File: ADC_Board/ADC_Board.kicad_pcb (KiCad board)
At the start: 2 copper layers, 96 x 67.5 mm, 55 parts, among them IC1 UCC12040DVE, IC2 ADS131M04QPWRQ1, IC7 ISO7762FDWR, J1 Conn_01x01_Pin, J2 Conn_01x01_Pin, J3 Conn_01x01_Pin, J4 Conn_01x01_Pin, J5 Conn_01x01_Pin, J6 Conn_01x01_Pin, J7 Conn_01x01_Pin, J8 Conn_01x01_Pin, U1 OPA990IDCKR, U2 OPA990IDCKR, U3 INA210AIDCKR, U4 INA210AIDCKR, U5 Nucleo_L432KC

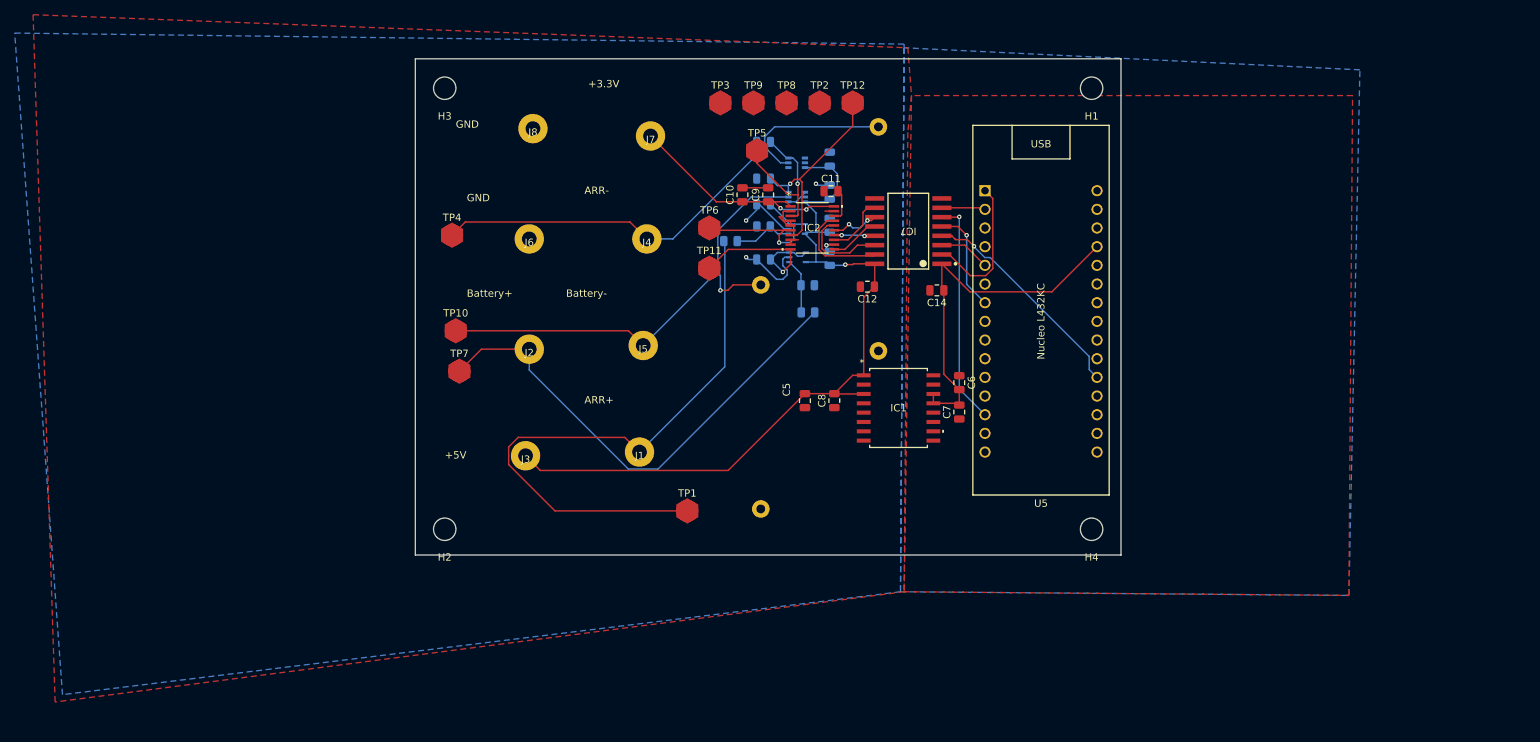
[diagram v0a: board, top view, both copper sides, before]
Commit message: final iteration of schematic before printing
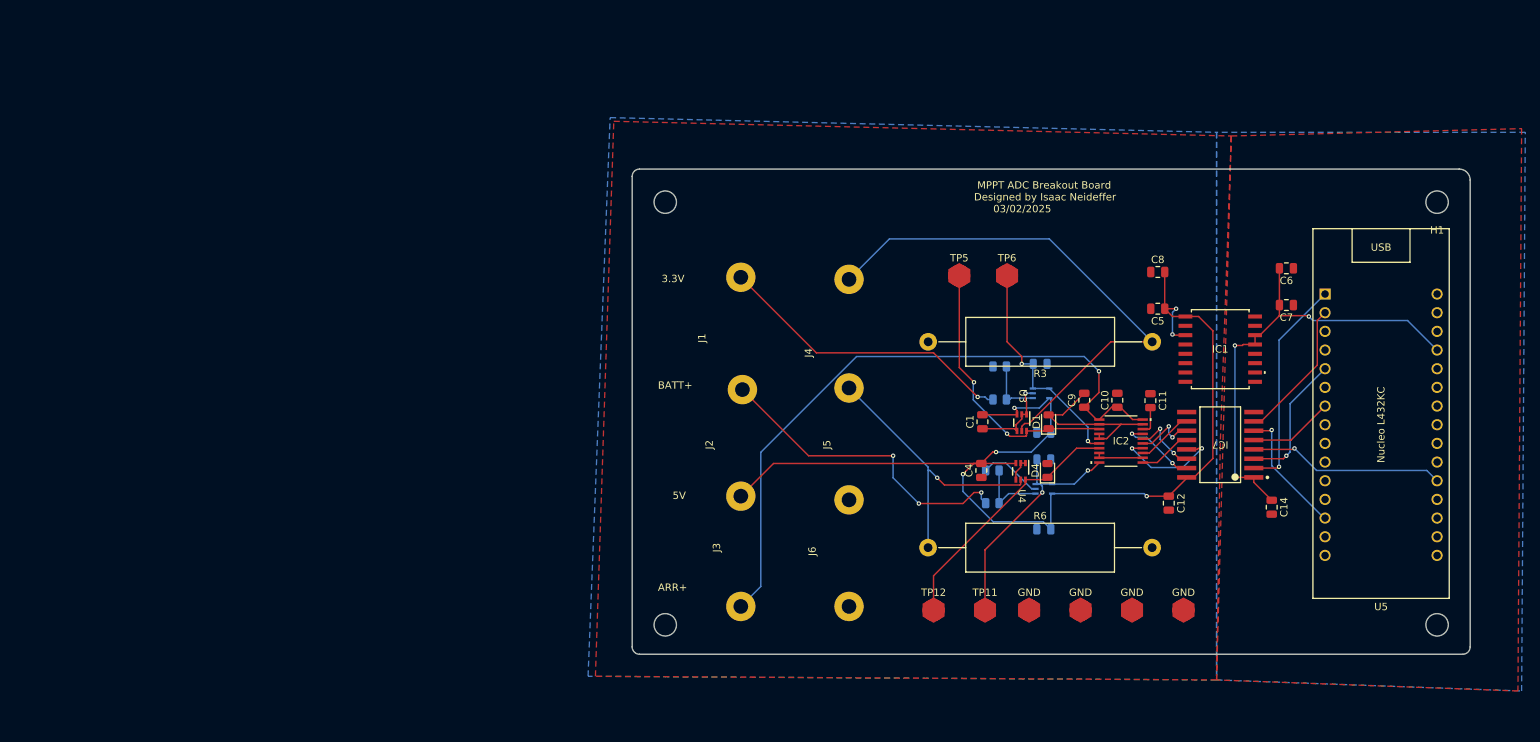
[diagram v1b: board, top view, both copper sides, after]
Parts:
- removed TP1: +ARR_TP, UTSVT_Special:TestPoint_HEX_3mmID
- removed TP10, TP2, TP3, TP8: GND_TP, UTSVT_Special:TestPoint_HEX_3mmID
- removed TP4: -ARR_TP, UTSVT_Special:TestPoint_HEX_3mmID
- removed TP7: +BATT_TP, UTSVT_Special:TestPoint_HEX_3mmID
- removed TP9: -BATT_TP, UTSVT_Special:TestPoint_HEX_3mmID
- added GND: GND_TP, UTSVT_Special:TestPoint_HEX_3mmID, F.Cu at (227.0, 93.5)
- added GND: -BATT_TP, UTSVT_Special:TestPoint_HEX_3mmID, F.Cu at (220.0, 93.5)
- added GND: GND_TP, UTSVT_Special:TestPoint_HEX_3mmID, F.Cu at (234.0, 93.5)
- added GND: GND_TP, UTSVT_Special:TestPoint_HEX_3mmID, F.Cu at (213.0, 93.5)
- C1, C4, D1, D4, R3, R6, U3, U4: moved to F.Cu
- moved H2 135.6 mm to (268.5, 95.5)
- moved J8 77.9 mm to (188.5, 93.0), turned to 90 degrees
- moved TP12 69.9 mm to (200.0, 93.5)
- moved J7 65.2 mm to (173.8, 93.0), turned to 90 degrees
- moved TP11 59.7 mm to (207.0, 93.5)
- moved H4 59.4 mm to (163.5, 95.5)
- moved C10 58.2 mm to (225.0, 65.0)
- moved J6 56.1 mm to (188.5, 78.5), turned to 90 degrees
- moved D4 55.4 mm to (215.5, 74.5), turned to 90 degrees
- moved D1 54.3 mm to (215.7, 67.9), turned to 90 degrees
- moved C3 54.3 mm to (215.0, 82.5), turned to 0 degrees
- moved C14 54.3 mm to (246.0, 79.5), turned to -90 degrees
- moved C11 52.0 mm to (229.5, 65.0), turned to -90 degrees
- moved IC7 51.4 mm to (239.0, 71.0)
- moved C9 51.3 mm to (220.5, 65.0)
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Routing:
- net +3.3V: track 32.6 -> 90.1 mm, vias 2 -> 1
- net +5V: track 108.0 -> 152.2 mm, vias 1 -> 6
- net /ARR+: track 82.0 -> 41.2 mm, vias 0 -> 1
- net /BATTERY-: track 66.2 -> 40.3 mm
- net /BATTERY+: track 66.8 -> 43.0 mm, vias 0 -> 3
- net /ARRAY_CURRENT+: track 22.1 -> 37.8 mm, vias 1 -> 2
- net GND: track 38.8 -> 54.2 mm, vias 4 -> 1
- net /DRDY_I: track 5.96 -> 19.4 mm
- net /MISO_I: track 30.8 -> 17.5 mm
- net +5V_I: track 50.3 -> 63.0 mm, vias 0 -> 3
- net /MOSI_I: track 7.01 -> 18.6 mm, vias 0 -> 1
- net /BATTERY_VOLTAGE+: track 23.6 -> 34.4 mm, vias 1 -> 2
- net /ADC_DRIVER_CLK_I: track 19.6 -> 29.6 mm, vias 0 -> 1
- net /SPI_CLOCK: track 5.61 -> 15.2 mm
- net /BATTERY_CURRENT+: track 27.9 -> 34.7 mm, vias 1 -> 0
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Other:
- board size 96 x 67.5 mm -> 114 x 66 mm
- board text added: "3.3V"
- board text added: "5V"
- board text added: "BATT+"
- board text added: "MPPT ADC Breakout Board Designed by Isaac Neideffer 03/02/2025"
- board text removed: "+3.3V"
- board text removed: "+5V"
- board text removed: "ARR-"
- board text removed: "Battery+"
- board text removed: "Battery-"
- board text removed: "GND"

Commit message: made changes to layout and schematic
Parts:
- removed GND (x3): GND_TP, UTSVT_Special:TestPoint_HEX_3mmID
- removed GND: -BATT_TP, UTSVT_Special:TestPoint_HEX_3mmID
- removed J3, J6, J7, J8: Conn_01x01_Pin, UTSVT_Connectors:Banana_Jack_1_Pin_4mm
- added C13: 33u, Capacitor_SMD:C_0805_2012Metric, F.Cu at (187.2, 63.5)
- added C15: 0.47u, Capacitor_SMD:C_0805_2012Metric, F.Cu at (183.7, 63.5)
- added D5: Power_LED, LED_SMD:LED_0805_2012Metric, F.Cu at (195.1, 65.5)
- added F1: Fuse, Fuse:Fuseholder_Blade_Mini_Keystone_3568, F.Cu at (167.2, 57.5)
- added F2: Fuse, Fuse:Fuseholder_Blade_Mini_Keystone_3568, F.Cu at (163.8, 85.0)
- added R7: 3k, Resistor_SMD:R_1206_3216Metric_Pad1.30x1.75mm_HandSolder, F.Cu at (194.9, 61.5)
- added U6: LM3940IMP-3.3, LM3940:MP04A, F.Cu at (185.5, 58.0)
- C5: value 10u -> 0.1u
- C6: value 0.1u -> 10u
- R1, R2, R4, R5: footprint Resistor_SMD:R_0805_2012Metric -> Resistor_SMD:R_1206_3216Metric_Pad1.30x1.75mm_HandSolder
- R3, R6: footprint Resistor_THT:R_Axial_Power_L20.0mm_W6.4mm_P30.48mm -> Resistor_SMD:R_1206_3216Metric
- moved H1 120.0 mm to (150.0, 57.0)
- moved H4 71.8 mm to (235.0, 102.0)
- moved C7 66.3 mm to (193.0, 89.0), turned to -90 degrees
- moved H3 65.4 mm to (150.0, 102.0)
- moved C8 59.0 mm to (193.0, 93.0), turned to 90 degrees
- moved R3 58.4 mm to (173.4, 72.4), turned to 90 degrees
- moved C6 58.4 mm to (208.0, 89.5), turned to 90 degrees
- moved H2 51.0 mm to (235.0, 57.0)
- moved J4 49.9 mm to (153.9, 84.5), turned to 0 degrees
- moved IC1 49.4 mm to (200.5, 89.0), turned to 180 degrees
- moved C5 49.2 mm to (206.5, 95.5)
- moved U5 42.1 mm to (220.9, 81.3)
- moved C9 41.9 mm to (179.5, 73.5), turned to -90 degrees
- moved IC2 40.7 mm to (185.0, 75.0)
- moved C11 39.7 mm to (190.5, 72.5)
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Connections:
- C5 pad 1: +5V -> GND_I
- C5 pad 2: GND -> +5V_I
- C6 pad 1: GND_I -> +5V_I
- C6 pad 2: +5V_I -> GND_I
- C7 pad 1: GND_I -> GND
- C7 pad 2: +5V_I -> +5V
- IC1 pad 1: +5V -> +5V_I
- IC1 pad 10: GND_I -> GND
- IC1 pad 11: GND_I -> GND
- IC1 pad 12: GND_I -> GND
- IC1 pad 13: +5V_I -> +5V
- IC1 pad 14: +5V_I -> +5V
- IC1 pad 15: GND_I -> GND
- IC1 pad 16: GND_I -> GND
- IC1 pad 2: GND -> GND_I
- IC1 pad 3: +5V -> +5V_I
- IC1 pad 4: GND -> GND_I
- IC1 pad 6: GND -> GND_I
- IC1 pad 7: GND -> GND_I
- IC1 pad 8: GND -> GND_I
- IC1 pad 9: GND_I -> GND
- R1 pad 2: /ARR+ -> /ARR+_IN
- R4 pad 2: /BATTERY+ -> /BATT+_IN
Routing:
- net +3.3V: track 90.1 -> 19.8 mm, vias 1 -> 0
- net +5V: track 152.2 -> 94.6 mm, vias 6 -> 5
- net /ARR-: track 72.5 -> 32.2 mm
- net /BATTERY+: track 43.0 -> 15.1 mm, vias 3 -> 0
- net /ARR+: track 41.2 -> 22.5 mm, vias 1 -> 0
- net /BATTERY-: track 40.3 -> 21.8 mm, vias 1 -> 0
- net /ARRAY_CURRENT+: track 37.8 -> 24.4 mm
- net /ARR+_IN: track 0.00 -> 8.84 mm
- net /ADC_DRIVER_CLK_I: track 29.6 -> 21.4 mm
- net /MISO_I: track 17.5 -> 25.5 mm
- net /BATT+_IN: track 0.00 -> 7.80 mm
- net +5V_I: track 63.0 -> 55.4 mm, vias 3 -> 0
- net /DRDY_I: track 19.4 -> 11.8 mm
- net /MOSI_I: track 18.6 -> 11.6 mm
- net /SPI_CLOCK: track 15.2 -> 9.35 mm
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- removed copper zone on B.Cu, net GND_I
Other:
- board size 114 x 66 mm -> 93 x 53.4 mm
- board text added: "ARRAY+"
- board text added: "ARRAY-"
- board text added: "BATTERY+"
- board text added: "BATTERY-"
- board text removed: "3.3V"
- board text removed: "5V"
- board text removed: "ARR+"
- board text removed: "BATT+"
- board text removed: "MPPT ADC Breakout Board Designed by Isaac Neideffer 03/02/2025"

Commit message: Addressed Ravi's Review
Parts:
- added D6: 3.3v_LED, LED_SMD:LED_0805_2012Metric, F.Cu at (192.4, 62.4)
- added J3: Conn_01x08_Pin, Connector_PinHeader_2.54mm:PinHeader_1x08_P2.54mm_Vertical, F.Cu at (204.8, 51.5)
- added J6: Conn_01x08_Pin, Connector_PinHeader_2.54mm:PinHeader_1x08_P2.54mm_Vertical, F.Cu at (196.9, 51.0)
- added R8: 2k, Resistor_SMD:R_1206_3216Metric_Pad1.30x1.75mm_HandSolder, F.Cu at (187.9, 62.2)
- added TP1: TestPoint, UTSVT_Special:TestPoint_HEX_3mmID, F.Cu at (181.4, 51.0)
- added TP2: TestPoint, UTSVT_Special:TestPoint_HEX_3mmID, F.Cu at (185.4, 51.0)
- added TP3: TestPoint, UTSVT_Special:TestPoint_HEX_3mmID, F.Cu at (184.5, 83.7)
- added TP4: TestPoint, UTSVT_Special:TestPoint_HEX_3mmID, F.Cu at (187.4, 88.0)
- added TP7: TestPoint, UTSVT_Special:TestPoint_HEX_3mmID, F.Cu at (233.4, 72.2)
- added TP8: TestPoint, UTSVT_Special:TestPoint_HEX_3mmID, F.Cu at (233.5, 66.9)
- D5: value Power_LED -> 5v_LED
- U6: footprint LM3940:MP04A -> LM390:MP04A
- moved R7 7.52 mm to (187.9, 58.6)
- moved D5 7.41 mm to (192.6, 58.5), turned to 180 degrees
- moved H1 4.60 mm to (150.0, 52.4)
- moved H2 4.50 mm to (235.0, 52.5)
- moved TP6 4.30 mm to (175.2, 56.6)
- moved U6 4.28 mm to (181.2, 58.1)
- moved C13 4.28 mm to (183.0, 63.6)
- moved C15 4.28 mm to (179.5, 63.6)
- moved TP5 3.30 mm to (171.2, 56.6)
- moved IC2 0.05 mm to (184.9, 75.0)
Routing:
- net +5V_I: track 55.4 -> 92.6 mm
- net /ADC_DRIVER_CLK: track 11.4 -> 41.2 mm, vias 2 -> 3
- net /ADC_DRIVER_CLK_I: track 21.4 -> 50.8 mm
- net /MOSI_I: track 11.6 -> 36.7 mm
- net /MOSI: track 10.9 -> 35.5 mm, vias 2 -> 3
- net /SPI_CLOCK: track 9.35 -> 30.7 mm
- net /SPI_CLOCK_I: track 28.4 -> 49.4 mm
- net +3.3V: track 19.8 -> 38.0 mm, vias 0 -> 2
- net /SYNC/RESET: track 8.63 -> 26.5 mm
- net /SYNC/RESET_I: track 9.17 -> 26.1 mm
- net /MISO: track 8.08 -> 21.8 mm
- net /MISO_I: track 25.5 -> 38.3 mm
- net /DRDY_I: track 11.8 -> 22.8 mm
- net /DRDY: track 9.73 -> 19.3 mm
- net +5V: track 94.6 -> 101.0 mm
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- added copper zone on B.Cu, net GND_I
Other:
- board size 93 x 53.4 mm -> 93 x 57.7 mm

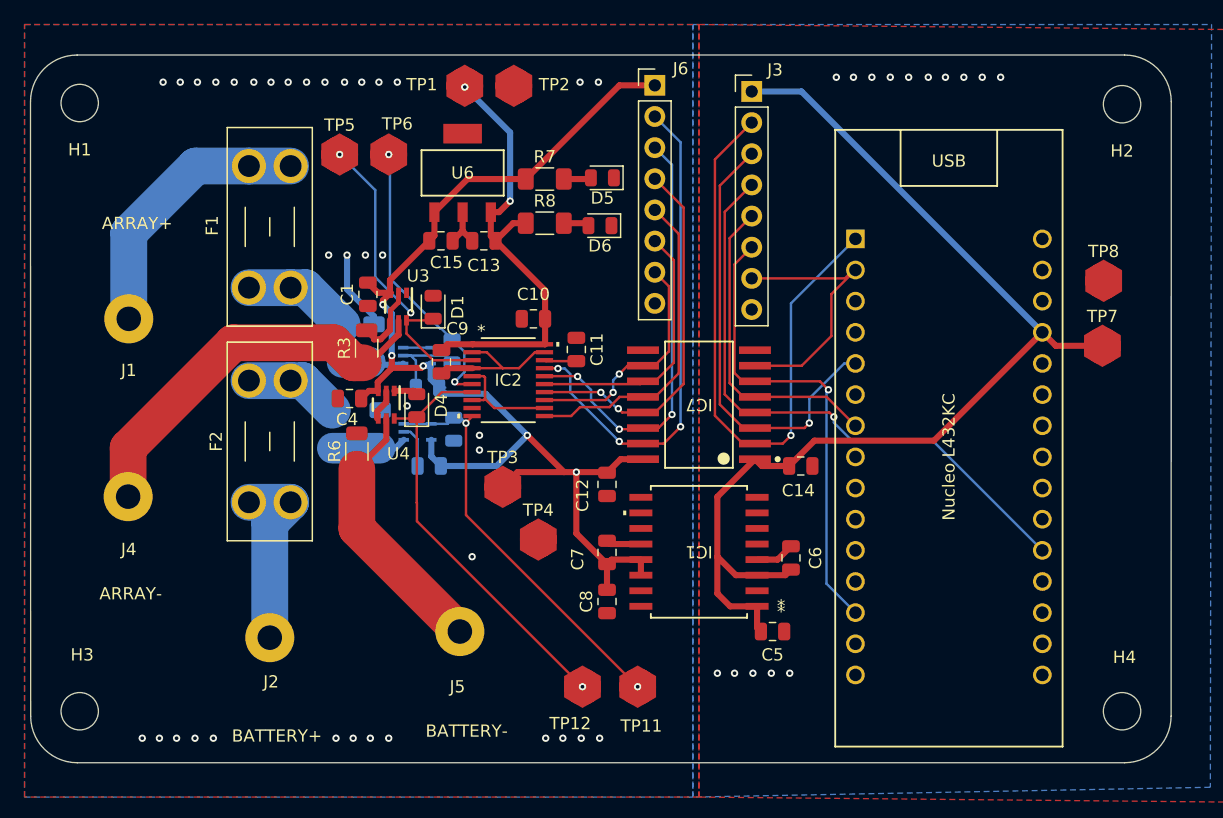
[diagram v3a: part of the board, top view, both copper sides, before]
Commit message: Fixed LDO pad, moved bypass caps, added more stitching vias, and cleaned up some silkscreen stuff
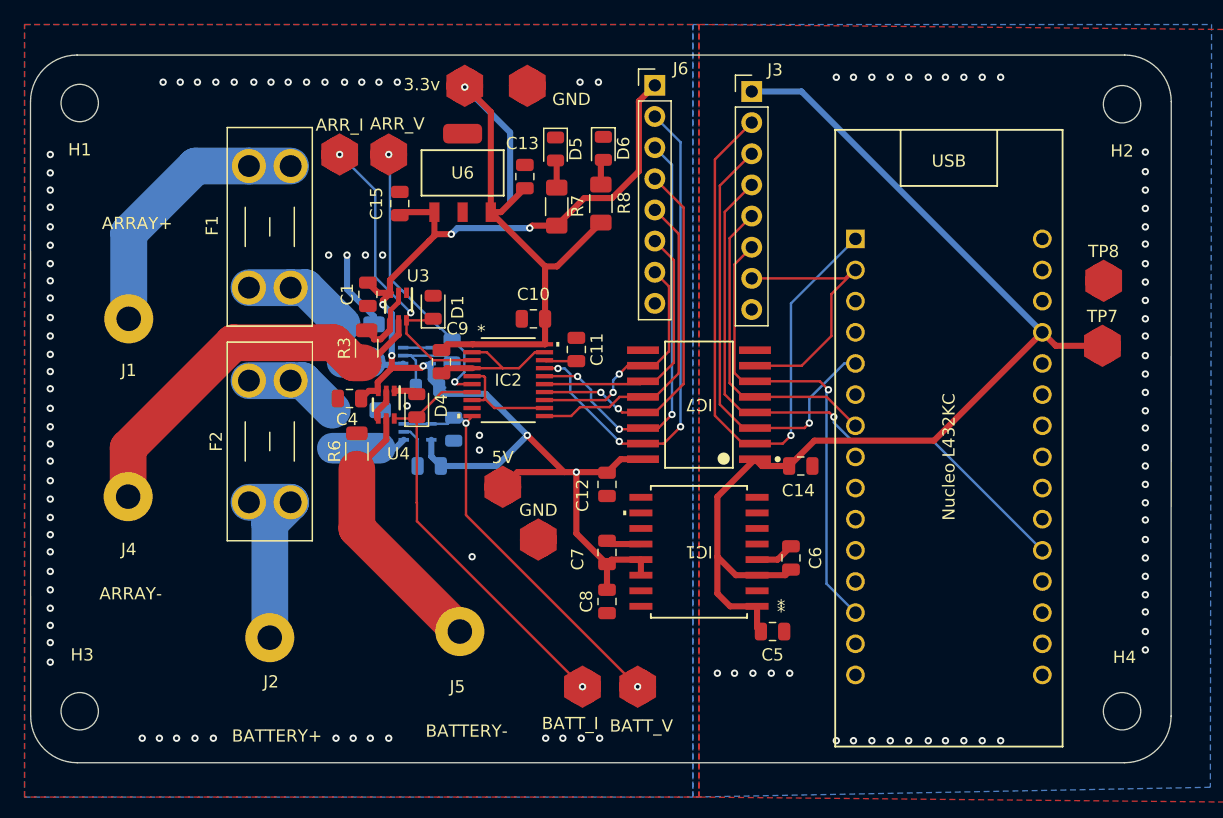
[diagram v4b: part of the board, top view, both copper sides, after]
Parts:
- moved D6 6.31 mm to (192.7, 56.1), turned to -90 degrees
- moved C13 6.21 mm to (186.3, 58.4), turned to 90 degrees
- moved R8 4.85 mm to (192.5, 60.6), turned to 90 degrees
- moved C15 4.53 mm to (176.1, 60.6), turned to 90 degrees
- moved D5 4.49 mm to (188.8, 56.1), turned to -90 degrees
- moved R7 2.45 mm to (188.9, 60.9), turned to 90 degrees
- moved GND 1.10 mm to (186.5, 51.0)
- renumbered TP1 to 3.3v, TP3 to 5V, TP5 to ARR_I, TP6 to ARR_V, TP12 to BATT_I, TP11 to BATT_V, TP2 to GND, TP4 to GND
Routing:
- net +3.3V: track 38.0 -> 53.2 mm, vias 2 -> 1
- net +5V: track 101.0 -> 108.0 mm, vias 5 -> 7
- net GND: track 56.4 -> 52.5 mm, vias 37 -> 66
- net GND_I: vias 15 -> 53
